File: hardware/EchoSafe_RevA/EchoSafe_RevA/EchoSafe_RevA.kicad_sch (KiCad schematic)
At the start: 20 parts, among them M1 C0720B001F, M2 C0720B001F, M3 C0720B001F, M4 C0720B001F, U1 ESP32-S3-WROOM-1-N16R8, U2 MAX98357AETE+T, U3 DRV2605LDGS, U4 NPM1300-QEAA-R7

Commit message: Add TCA9548A mux + 3 more DRV2605 chips to RevA schematic, fix sym-lib-table
- Added TCA9548A (U5, 24-pin TSSOP) to the schematic's embedded symbol
  library, pinout taken directly from TI datasheet SCPS207F (not memory) —
  A0/A1/A2/RESET/SDA/SCL on the left, SD0-7/SC0-7 channel pairs on the
  right, VCC/GND top/bottom. Verified: pin count, uuid uniqueness, and
  reference-designator uniqueness all check out; parenthesis balance of
  the whole .kicad_sch is intact.
- Duplicated the existing working DRV2605LDGS instance three more times
  (U6, U7, U8) alongside the original U3, giving the 4 independent haptic
  drivers the firmware expects. Placed in open schematic space (x=255,
  y=40/75/110) clear of existing components.
- These 5 new parts are PLACED but NOT WIRED — no signal nets exist
  anywhere in this schematic yet (see CLAUDE.md), so connecting the mux
  to the ESP32's I2C bus and each DRV2605's channel is still open work.
- Fixed hardware/EchoSafe_RevA/EchoSafe_RevA/sym-lib-table: it pointed at
  nonexistent files in BOTH the original and consolidated copies (pre-
  existing bug, not introduced by consolidation), and 2 of 5 library
  nicknames didn't match the lib_id prefixes actually used by placed
  symbols. Now points at the real library files via ${KIPRJMOD}-relative
  paths with matching nicknames.

Co-Authored-By: Claude Sonnet 5 <noreply@anthropic.com>
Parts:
- added U5: TCA9548A, Package_SO:TSSOP-24_4.4x7.8mm_P0.65mm, symbol Driver_Haptic:TCA9548A
- added U6, U7, U8: DRV2605LDGS, Package_SO:VSSOP-10_3x3mm_P0.5mm, symbol Driver_Haptic:DRV2605LDGS

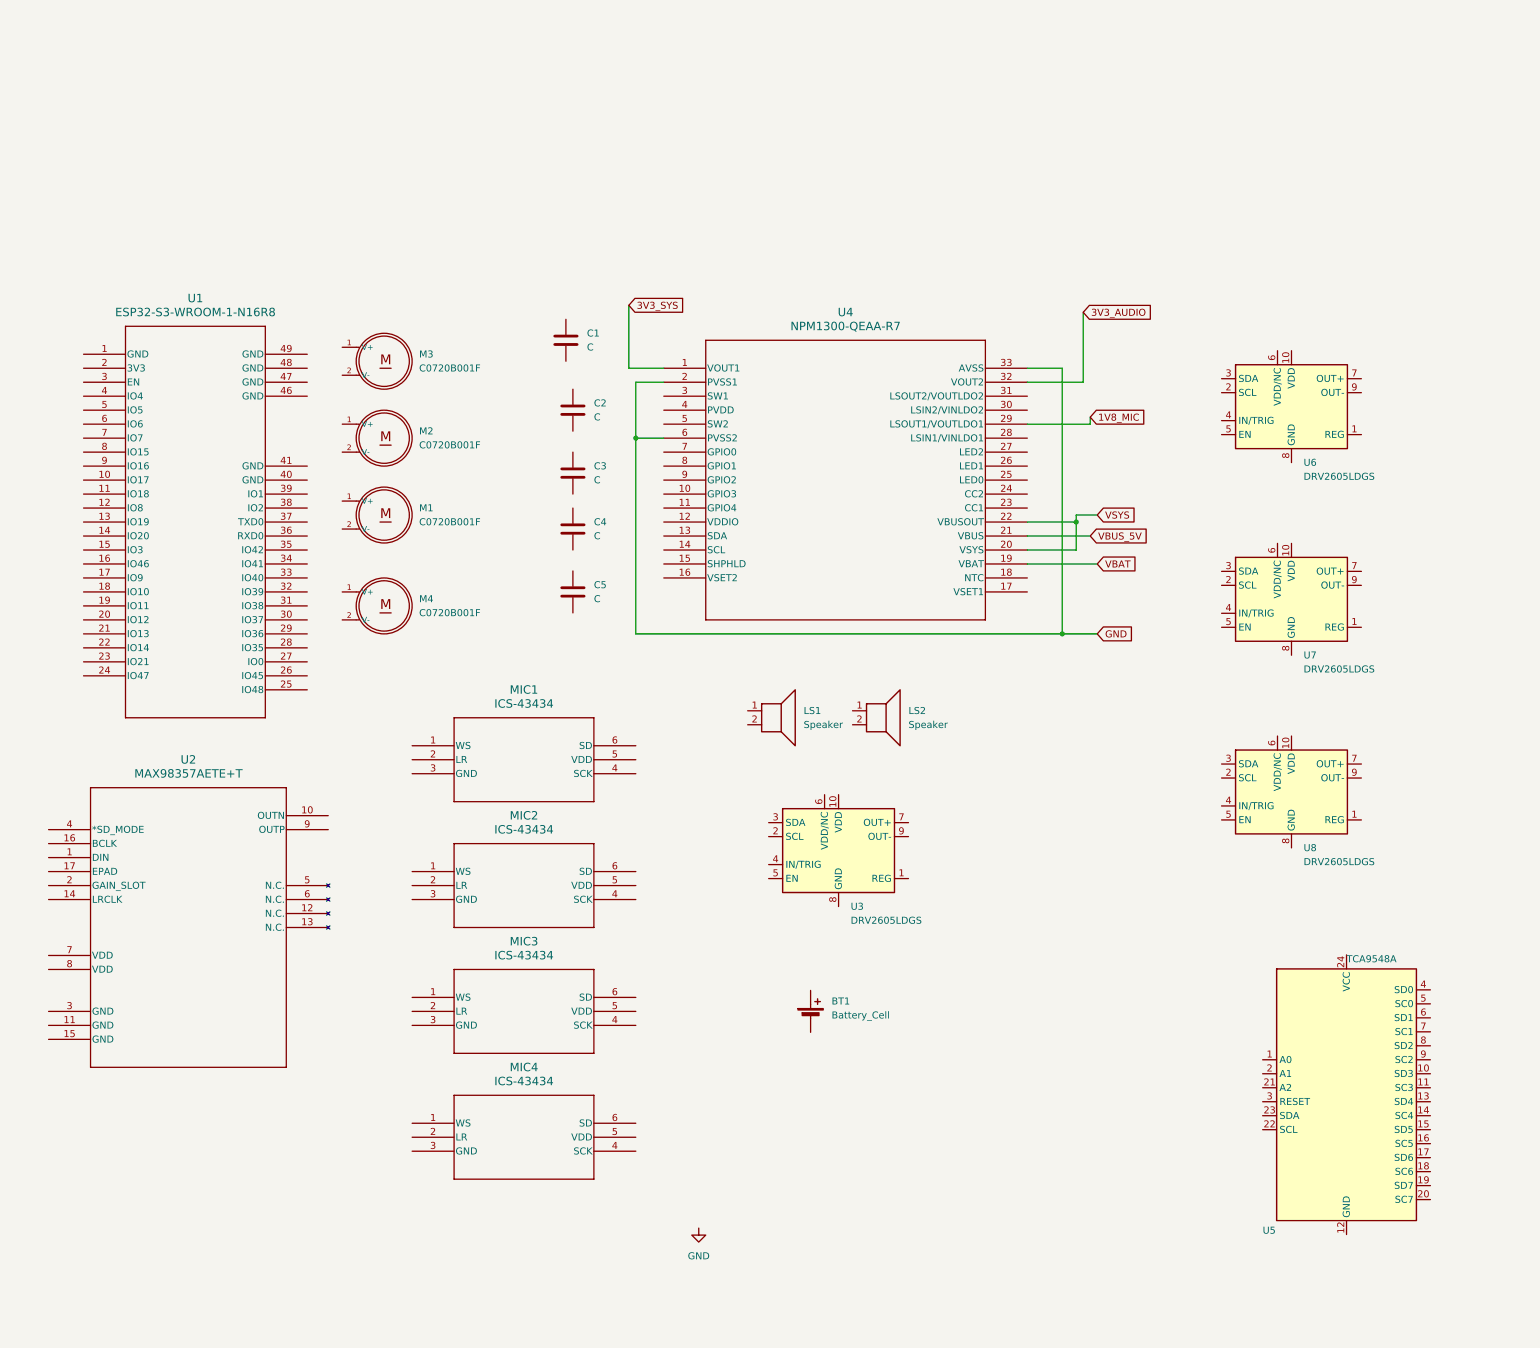
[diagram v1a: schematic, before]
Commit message: Wire I2S, I2C, and haptic-output signal nets in RevA schematic
Adds every signal net the firmware requires that was previously missing
entirely (schematic had only power rails wired, 0 signal nets):

- MIC_TOP_WS/SCK/SD and MIC_BOT_WS/SCK/SD: ESP32 <-> mic pairs (I2S0/I2S1)
- SPK_DIN/BCLK/LRCLK: ESP32 <-> MAX98357A
- HAPTIC_SDA/SCL: ESP32 <-> TCA9548A upstream I2C
- MUX_CH0-3_SDA/SCL: TCA9548A downstream channels <-> each DRV2605
- MOTOR_*_OUTP/OUTN: each DRV2605 <-> its haptic motor
- SPK_OUTP/OUTN: MAX98357A <-> both speakers (parallel)
- Power/enable ties: mic VDD/SEL, MAX98357A enable/VDD, DRV2605 EN/VDD/
  IN-TRIG, TCA9548A address/reset/VCC, all against existing rails
- no_connect markers on MAX98357A's true N.C. pins + GAIN_SLOT

Used global labels (matching the sheet's own power-rail convention)
placed directly at each pin's verified absolute coordinate, computed from
extracted symbol pin tables + placement data rather than eyeballed —
caught and corrected one transcription error (IO47 column) this way
before it reached the file. Verified post-insertion: whole-file paren
balance intact, 381 unique UUIDs, no coordinate collisions between
different net names.

Several judgment calls were required since nothing in the existing
schematic specified them (mic/motor quadrant assignment, which 3.3V rail
each IC uses, how unused pins are tied) — all documented in CLAUDE.md's
hardware section for verification against actual intent. One open gap
flagged rather than guessed: DRV2605 REG-pin decoupling caps not added.

Co-Authored-By: Claude Sonnet 5 <noreply@anthropic.com>
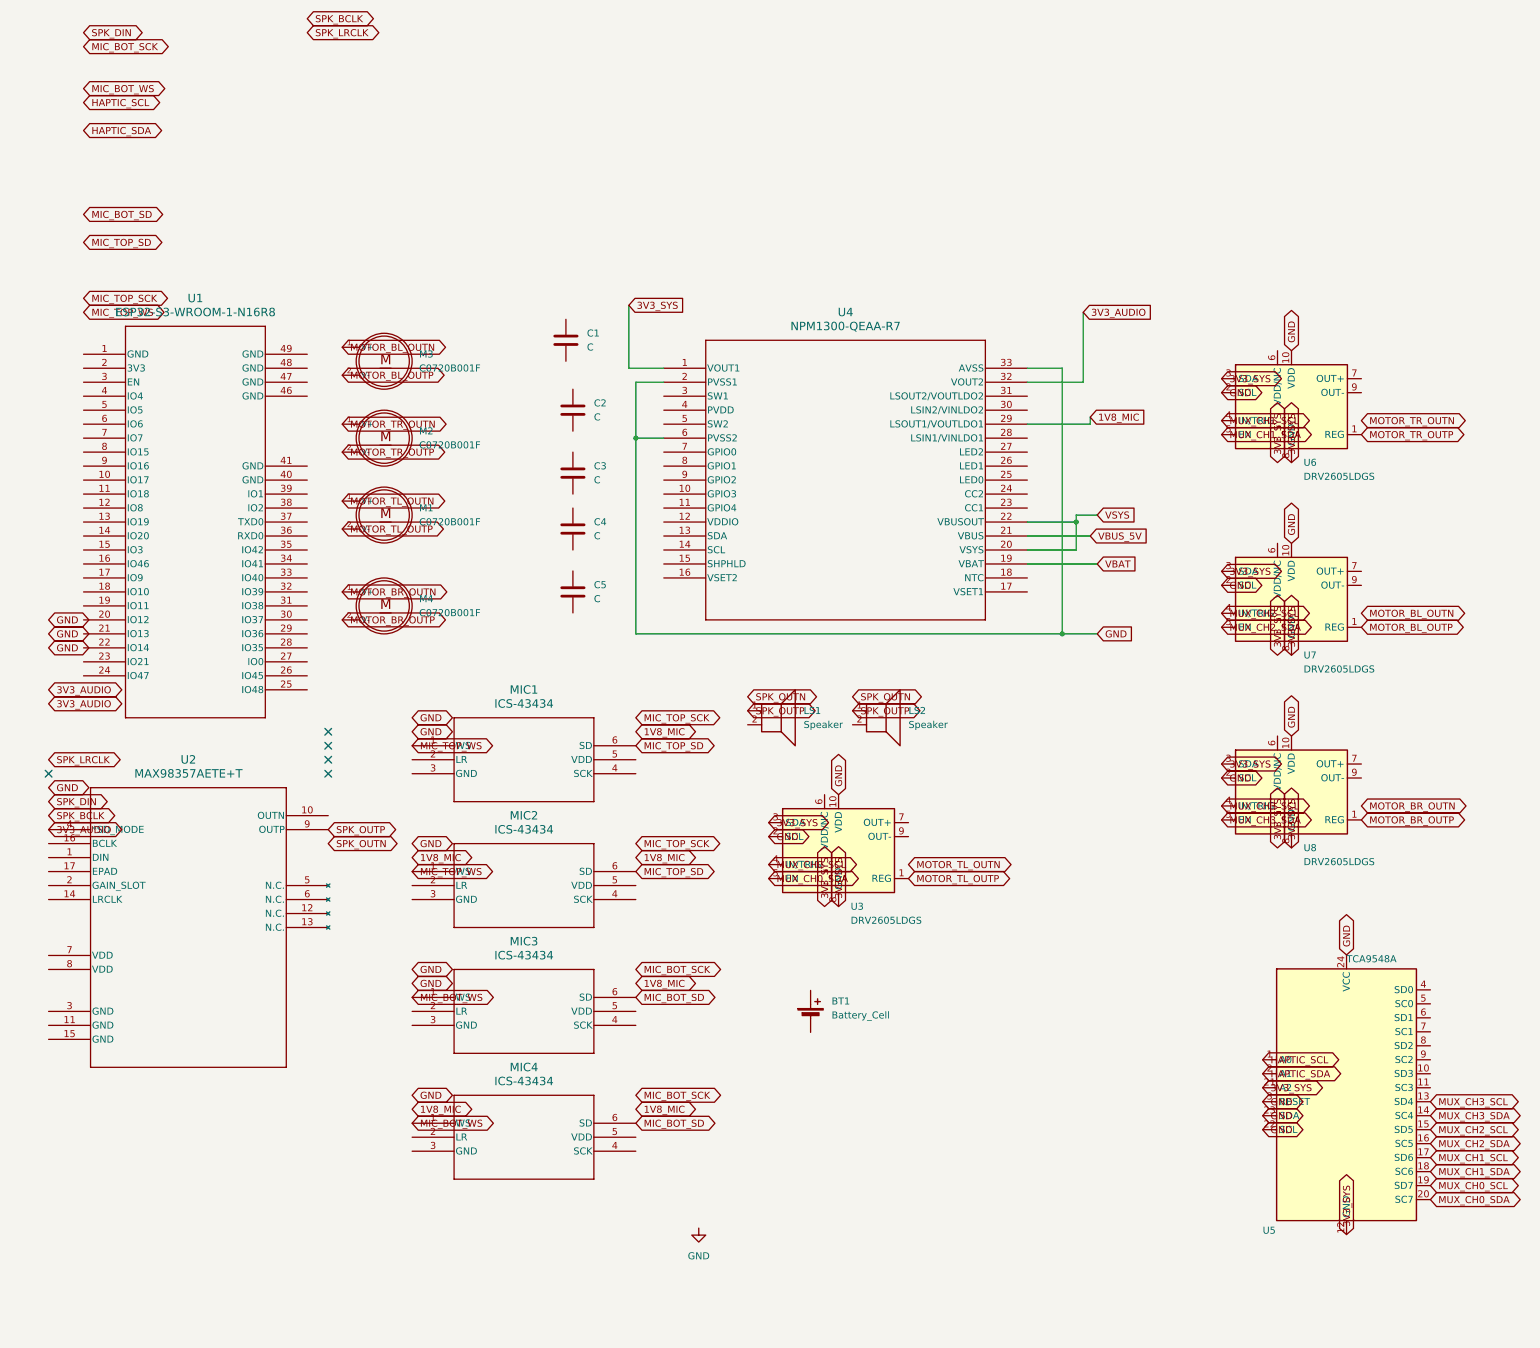
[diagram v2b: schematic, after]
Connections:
- net 3V3_AUDIO: now also U2.4 (*SD_MODE)
- net 3V3_SYS: now also U3.3 (SDA), U3.8 (GND), U5.12 (GND), U5.21 (A2), U6.3 (SDA), U6.8 (GND), U7.3 (SDA), U7.8 (GND), U8.3 (SDA), U8.8 (GND)
- net GND: now also U3.10 (VDD), U3.2 (SCL), U5.22 (SCL), U5.23 (SDA), U5.24 (VCC), U5.3 (RESET), U6.10 (VDD), U6.2 (SCL), U7.10 (VDD), U7.2 (SCL), U8.10 (VDD), U8.2 (SCL)
- net MOTOR_TR_OUTN: now reaches M2.1 (V+)
- net MOTOR_TR_OUTP: now reaches M2.2 (V-)
- net MOTOR_TR_OUTP: now also U6.1 (REG)
- net MOTOR_BR_OUTP: now reaches U8.1 (REG)
- net MOTOR_BR_OUTP: now also M4.2 (V-)
- net MUX_CH3_SCL: now reaches U8.4 (IN/TRIG)
- net MUX_CH3_SCL: now also U5.13 (SD4)
- net MUX_CH3_SDA: now reaches U8.5 (EN)
- net MUX_CH3_SDA: now also U5.14 (SC4)
- net MIC_TOP_WS: now reaches MIC1.1 (WS)
- net MIC_TOP_WS: now also MIC2.1 (WS)
- net MIC_TOP_SD: now reaches MIC1.6 (SD)
- net MIC_TOP_SD: now also MIC2.6 (SD)
- net MOTOR_BL_OUTP: now reaches U7.1 (REG)
- net MOTOR_BL_OUTP: now also M3.2 (V-)
- net MUX_CH2_SCL: now reaches U7.4 (IN/TRIG)
- net MUX_CH2_SCL: now also U5.15 (SD5)
- net MUX_CH2_SDA: now reaches U7.5 (EN)
- net MUX_CH2_SDA: now also U5.16 (SC5)
- net MOTOR_TL_OUTP: now reaches U3.1 (REG)
- net MOTOR_TL_OUTP: now also M1.2 (V-)
- net MUX_CH0_SCL: now reaches U3.4 (IN/TRIG)
- net MUX_CH0_SCL: now also U5.19 (SD7)
- net MUX_CH0_SDA: now reaches U3.5 (EN)
- net MUX_CH0_SDA: now also U5.20 (SC7)
- net MIC_BOT_WS: now reaches MIC4.1 (WS)
- net MIC_BOT_WS: now also MIC3.1 (WS)
- net MIC_BOT_SD: now reaches MIC4.6 (SD)
- net MIC_BOT_SD: now also MIC3.6 (SD)
- net MOTOR_BR_OUTN: now reaches M4.1 (V+)
- net SPK_OUTP: now reaches LS1.1
- net SPK_OUTP: now also LS2.1, U2.9 (OUTP)
- net MOTOR_BL_OUTN: now reaches M3.1 (V+)
- net MUX_CH1_SCL: now reaches U6.4 (IN/TRIG)
- net MUX_CH1_SCL: now also U5.17 (SD6)
- net MUX_CH1_SDA: now reaches U6.5 (EN)
- net MUX_CH1_SDA: now also U5.18 (SC6)
- net MOTOR_TL_OUTN: now reaches M1.1 (V+)
- net HAPTIC_SCL: now reaches U5.1 (A0)
- net HAPTIC_SDA: now reaches U5.2 (A1)
- no-connect marks 0 -> 5

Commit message: Add DRV2605 decoupling caps, fix mic/motor clockwise quadrant assignment
- Corrected MIC3/MIC4 and M3/M4 quadrant assignment: the initial guess
  (numeric order) was wrong. Actual layout is clockwise: MIC1/M1=TL,
  MIC2/M2=TR, MIC3/M3=BR, MIC4/M4=BL. Fixed by swapping MIC3/MIC4's SEL
  rail (1V8_MIC <-> GND) and renaming the motor-output labels at M3/M4 so
  U7 (mux channel 2, "Bottom-Left") now drives M4 and U8 (channel 3,
  "Bottom-Right") now drives M3 -- the driver-to-channel mapping itself
  didn't change, only which physical motor each driver reaches.
- Added C6/C7/C8/C9 (0.1uF), one per DRV2605 (U3/U6/U7/U8), each wired
  directly from the driver's REG pin to GND per datasheet recommendation.
- Decided to keep the 1-amp/2-parallel-speaker architecture rather than
  adding a second MAX98357A -- documented reasoning and the speaker-
  impedance caveat (needs 8 ohm speakers) in CLAUDE.md.

Verified post-edit: whole-file paren balance intact, 401 unique UUIDs, no
duplicate reference designators, correct 2-endpoint count on every
affected net.

Co-Authored-By: Claude Sonnet 5 <noreply@anthropic.com>
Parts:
- added C6, C7, C8, C9: 0.1uF, symbol Device:C
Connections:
- net GND: now also C6.1, C7.1, C8.1, C9.1
- net MOTOR_BL_OUTN: now also M4.1 (V+); no longer M3.1 (V+)
- net MOTOR_BL_OUTP: now also M4.2 (V-); no longer M3.2 (V-)
- net MOTOR_BR_OUTN: now also M3.1 (V+); no longer M4.1 (V+)
- net MOTOR_BR_OUTP: now also M3.2 (V-); no longer M4.2 (V-)
- net at U8.7 (OUT+): now also C9.2
- net at U7.7 (OUT+): now also C8.2
- net at U3.7 (OUT+): now also C6.2
- net at U6.7 (OUT+): now also C7.2

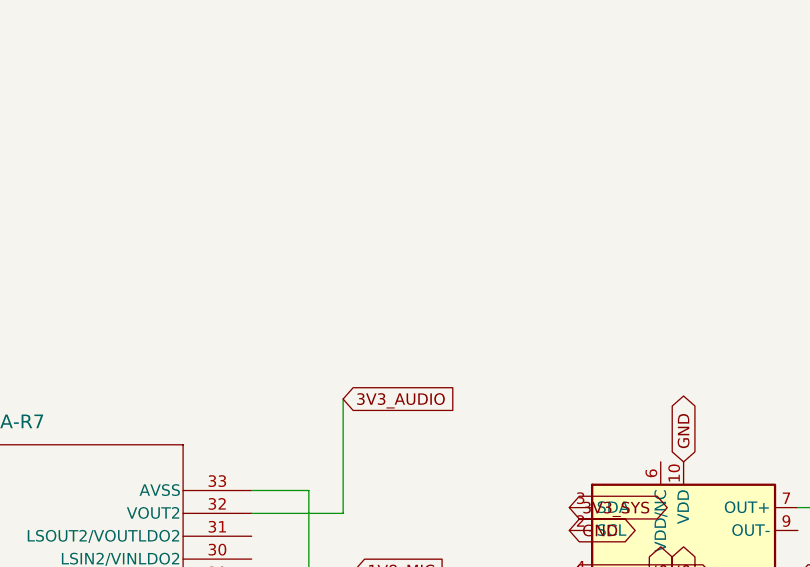
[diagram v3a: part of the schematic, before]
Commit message: Confirm speaker impedance, add USB-C charging connector
- Speaker impedance confirmed as 8 ohm: 2x8 ohm parallel = 4 ohm, within
  MAX98357A spec. 1-amp decision is now final, not conditional.
- Added J1, a placeholder USB-C connector (Connector:USB_C_Power_Only,
  embedded symbol -- no real part/footprint chosen yet) exposing VBUS,
  GND, CC1, CC2, SHIELD. Wired directly to the NPM1300 PMIC's own
  VBUS/CC1/CC2 pins (21/23/24) -- no external CC pull-down resistors,
  since the nPM1300 has built-in USB-C/BC1.2 detection on those pins per
  its standard reference design. Flagged in CLAUDE.md that this one relies
  on general knowledge of the chip family rather than a freshly-fetched
  datasheet, unlike TCA9548A earlier this session.
- No power switch or button added -- confirmed out of scope after
  reviewing (and mostly discarding) two old reference images. EchoSafe.png
  is the real target look, minus the in-ear-bud cable; the mechanical
  layout concept PNG was outdated and disregarded per feedback.

Verified: whole-file paren balance intact, 415 unique UUIDs, no duplicate
references, correct 2-endpoint count on every new net.

Co-Authored-By: Claude Sonnet 5 <noreply@anthropic.com>
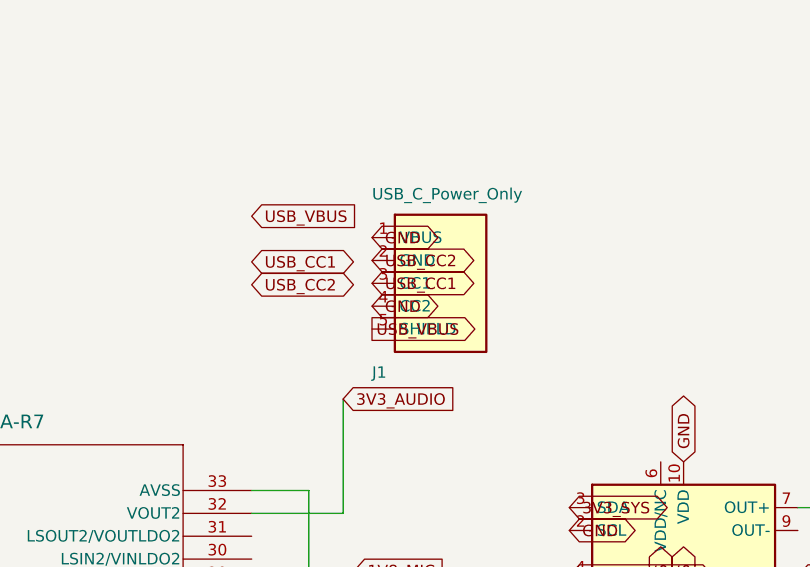
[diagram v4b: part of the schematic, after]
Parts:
- added J1: USB_C_Power_Only, symbol Connector:USB_C_Power_Only
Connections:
- net GND: now also J1.1 (VBUS), J1.4 (CC2)
- new net USB_CC1: J1.3 (CC1)
- new net USB_CC2: J1.2 (GND)
- new net USB_VBUS: J1.5 (SHIELD)

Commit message: Replace NPM1300 with TP4056+LD1117V33, add full capacitor BOM, confirm board partition
Major power architecture rework per user-supplied BOM:

- Removed NPM1300 PMIC entirely (lib_symbol def, instance, all 21 of its
  original wire segments, and the 7 power-rail labels that only served
  it) -- confirmed before deleting that it was never actually wired even
  in the original pre-consolidation schematic, so nothing real was lost.
- Removed the placeholder USB-C connector added earlier this session
  (Connector:USB_C_Power_Only, J1) -- superseded by the real part.
- Added J1 = TP4056_Module (HiLetGo, w/ protection) and LD1 = LD1117V33
  (SparkFun breakout) as new embedded symbols, wired: BT1 <-> VBAT <-> J1,
  J1.OUT+ <-> VSYS <-> LD1.VIN, LD1.VOUT -> 3V3_SYS.
- Consolidated three previously-separate rails (3V3_SYS/3V3_AUDIO/
  1V8_MIC) into one 3V3_SYS rail from the single LD1117V33 -- mics moved
  from a planned 1.8V supply to 3.3V (within ICS-43434's spec).
- Implemented the full C1-C17 capacitor BOM: renumbered/revalued the 4
  existing DRV2605 REG caps (C5-C8, corrected 0.1uF -> 1.0uF to match
  TI's actual datasheet spec), repurposed the pre-existing orphaned
  C1-C4 as LD1117V33 in/out decoupling, added C9-C17 for mic/TCA9548A/
  MAX98357A/ESP32 decoupling and a VSYS bulk cap. Full purpose table in
  CLAUDE.md.
- Documented the confirmed board partition: 4 earpiece modules (front-L/
  front-R each with mic+motor+speaker, rear-L/rear-R with just mic+motor)
  plus 1 central pod holding everything else. Schematic is still one
  flat sheet -- splitting into per-board KiCad sheets is future work.

Caught and fixed a duplication bug mid-implementation (added new C1-C4
instances without first removing the old orphaned ones) before it was
committed. Verified: whole-file paren balance intact, 407 unique UUIDs,
no duplicate references, no dead (<2-endpoint) nets, no coordinate
conflicts between different net names.

Co-Authored-By: Claude Sonnet 5 <noreply@anthropic.com>
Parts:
- removed C5: C, symbol Device:C
- removed J1: USB_C_Power_Only, symbol Connector:USB_C_Power_Only
- removed U4: NPM1300-QEAA-R7, QFN32_5X5_NOR, symbol PowerM IC:NPM1300-QEAA-R7
- added C10, C11, C12, C13, C14, C17, C9: 1uF, symbol Device:C
- added C15: 100nF, symbol Device:C
- added C16: 10uF, symbol Device:C
- added J1: TP4056_Module, symbol Power:TP4056_Module
- added LD1: LD1117V33, symbol Regulator_Linear:LD1117V33
- C1, C2: value C -> 10uF
- C3, C4: value C -> 100nF
- C5: renamed from C6; value 0.1uF -> 1uF
- C6: renamed from C7; value 0.1uF -> 1uF
- C7: renamed from C8; value 0.1uF -> 1uF
- C8: renamed from C9; value 0.1uF -> 1uF
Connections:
- net 3V3_AUDIO is gone; now on net 3V3_SYS: U2.4 (*SD_MODE)
- net 3V3_SYS: now also C2.2, C4.2, C10.2, C11.2, C12.2, C13.2, C14.2, C15.2, C17.2, C9.2, LD1.2 (VOUT)
- net GND: now also C1.1, C2.1, C3.1, C4.1, C10.1, C11.1, C12.1, C13.1, C14.1, C15.1, C16.1, C17.1, C9.1, J1.1 (BAT+), J1.3 (OUT+)
- net VBAT: now also J1.2 (BAT-)
- net VSYS: now also C1.2, C3.2, C16.2, J1.4 (OUT-), LD1.3 (VIN)
